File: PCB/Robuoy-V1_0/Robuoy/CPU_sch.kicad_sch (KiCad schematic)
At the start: 50 parts, among them J2 USB_C_Receptacle_USB2.0_16P, J6 TO PUSH BUTTON, Q4 MMBT2222A, Q8 2N7002, Q9 2N7002, SW3 ~{BOOT}, SW4 ~{RESET}, U102 CP2104-F03-GMR, U103 ESP32-WROOM-32E_(visible_peri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, U2 USBLC6-2SC6

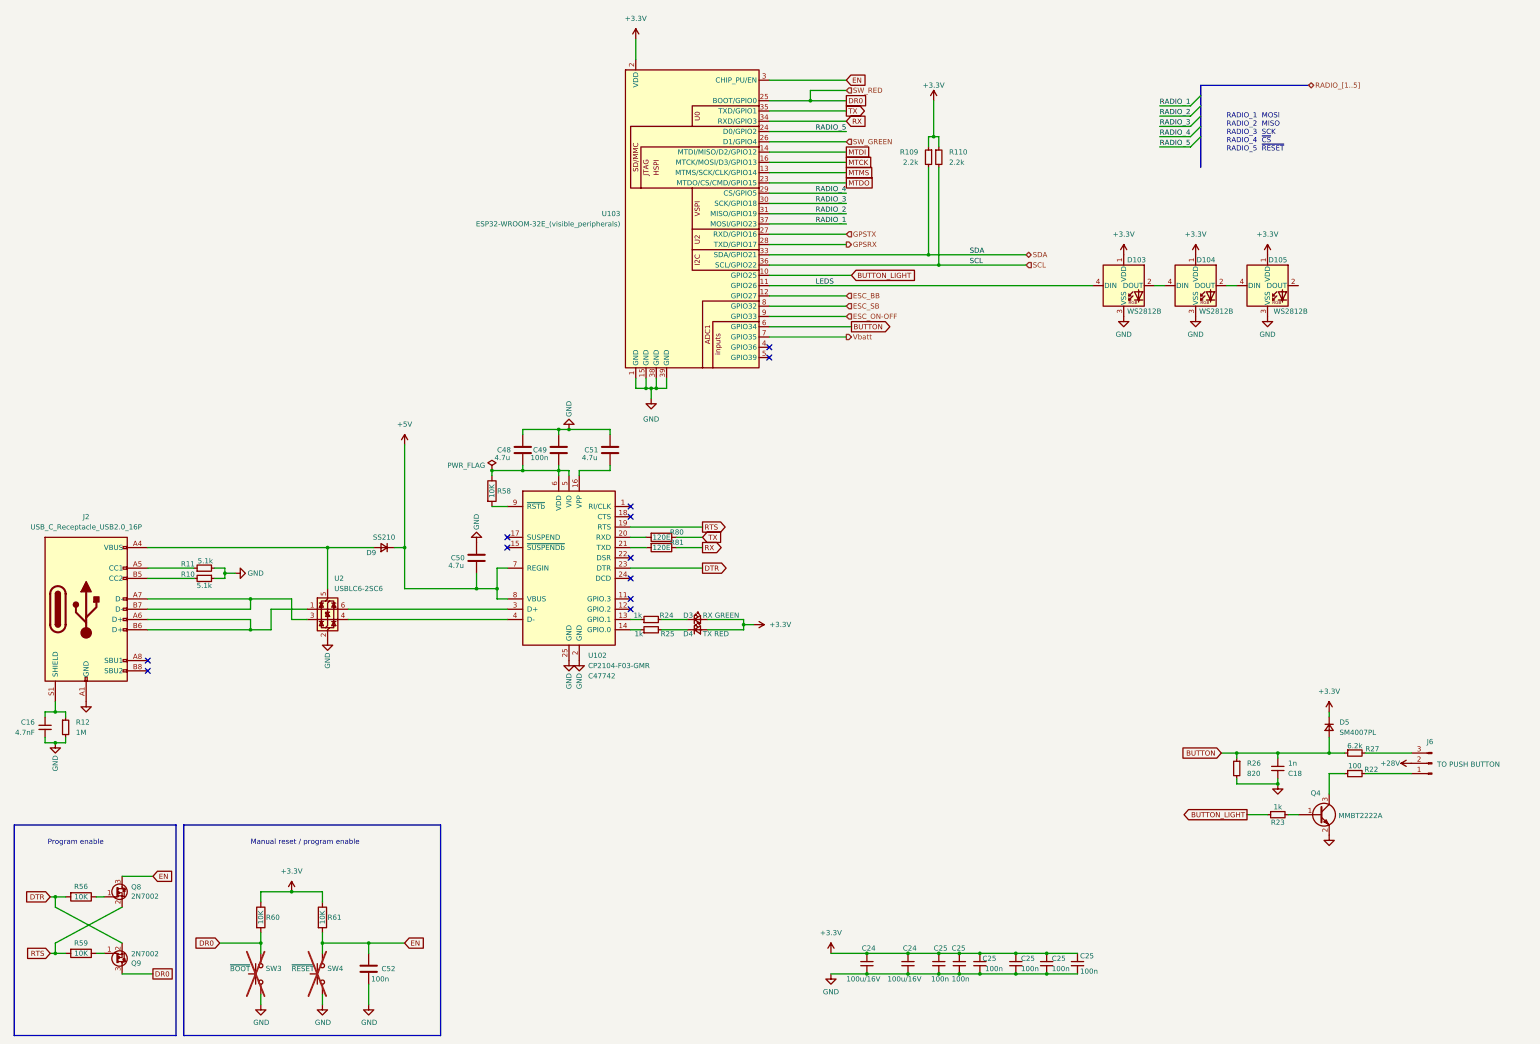
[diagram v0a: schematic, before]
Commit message: Schematics changed for new design
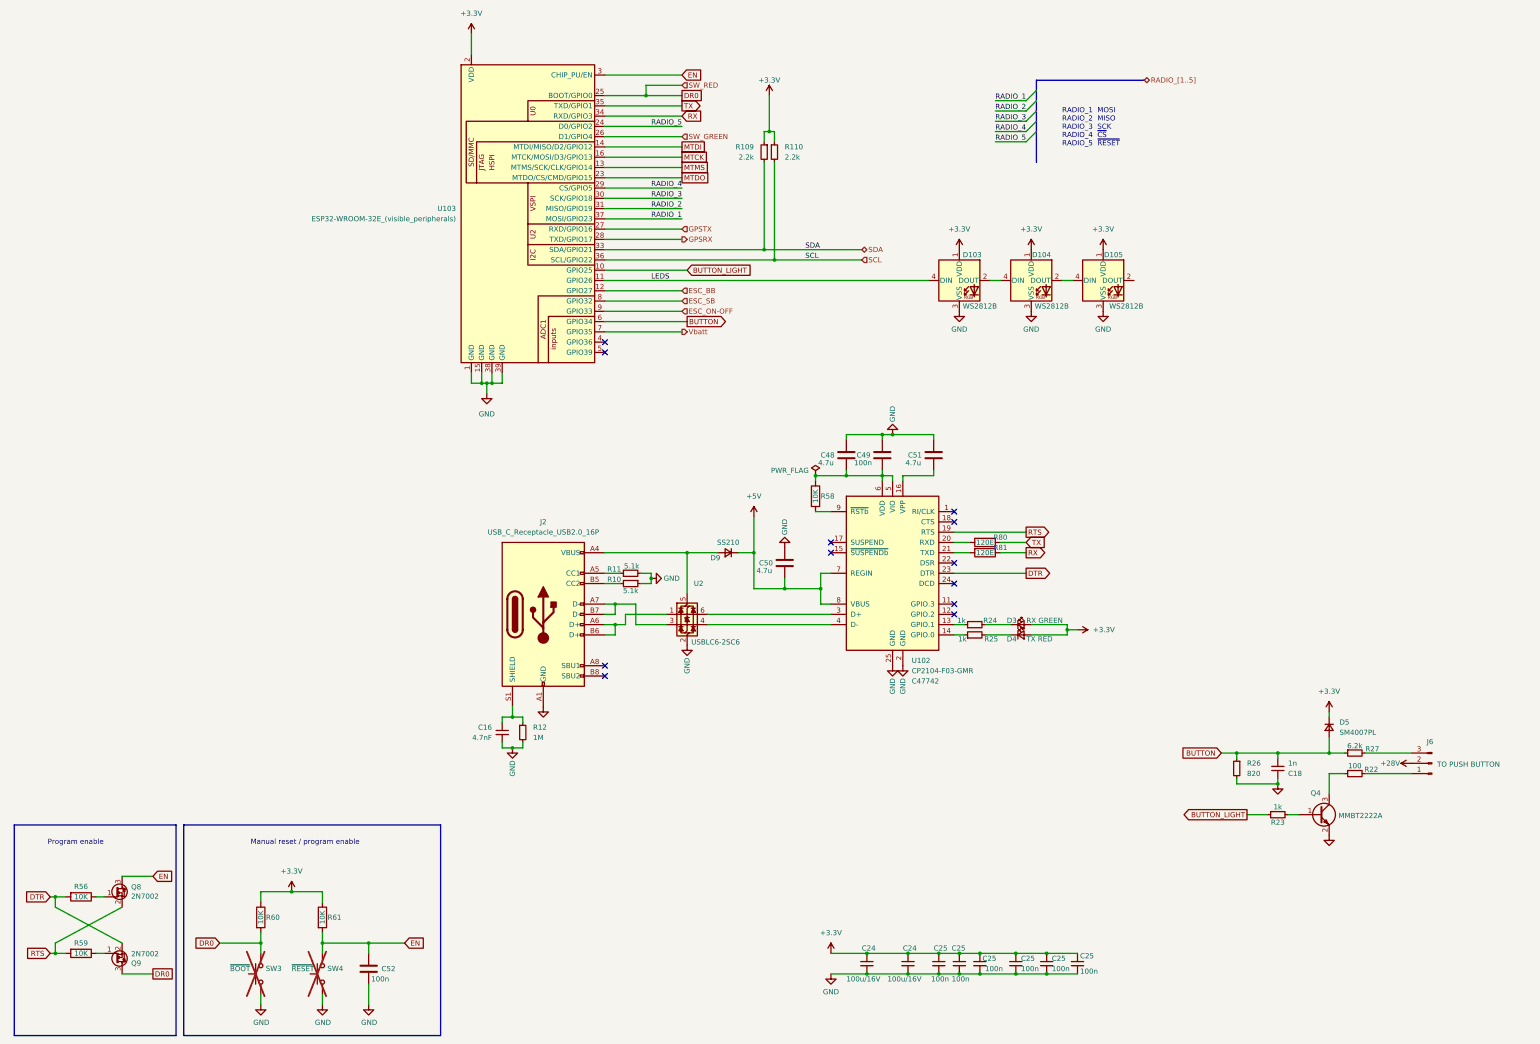
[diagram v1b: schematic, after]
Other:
- moved on the sheet: C16, C48, C49, C50, C51, D103, D104, D105, D3, D4, D9, J2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

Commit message: auto calibrate
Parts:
- removed C16: 4.7nF, symbol Device:C_Small
- removed C48, C50, C51: 4.7u, A_Device:C_0603, symbol Device:C
- removed C49: 100n, A_Device:C_0603, symbol Device:C
- removed D3: RX GREEN, A_Device:LED_0603, symbol Device:LED_Small
- removed D4: TX RED, A_Device:LED_0603, symbol Device:LED_Small
- removed D9: SS210, symbol Device:D_Small
- removed J2: USB_C_Receptacle_USB2.0_16P, symbol Connector:USB_C_Receptacle_USB2.0_16P
- removed Q8, Q9: 2N7002, A_IC_SOT:SOT-23_1.4x3_P0.95, symbol SmartBox4-0V1.2-rescue:NFET_small-AirSupplies-Repeater_4x_V1_0-rescue-Repeater_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
- removed R10, R11: 5.1k, symbol Device:R_Small
- removed R12: 1M, symbol Device:R_Small
- removed R24, R25: 1k, A_Device:R_0603, symbol Device:R_Small
- removed R56, R58, R59: 10K, A_Device:R_0603, symbol Device:R
- removed R80, R81: 120E, A_Device:R_0603, symbol Device:R
- removed U102: CP2104-F03-GMR, Package_DFN_QFN:QFN-24-1EP_4x4mm_P0.5mm_EP2.6x2.6mm, symbol Confocal:CP2104-F03-GMR
- removed U2: USBLC6-2SC6, Package_TO_SOT_SMD:SOT-23-6, symbol Power_Protection:USBLC6-2SC6
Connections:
- net DR0: now also D103.4 (DIN)
- net LEDS renamed SW_RED
- net SW_RED: no longer D103.4 (DIN)
- no-connect marks 12 -> 2
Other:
- note removed: "Program enable"
- moved on the sheet: C18, C24, C25, C52, D103, D104, D105, D5, J6, Q4, R109, R110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
